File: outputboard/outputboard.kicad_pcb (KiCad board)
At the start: 2 copper layers, 23.5 x 33.9 mm, 12 parts, among them J1 Conn_01x05_Male, J2 AudioJack4, Q1 2N2222A, SW1 SW_SPDT

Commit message: add part description for more complex parts, remove unused cap
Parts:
- D1: value LED_Dual_AAK -> LED_Dual_AAK 2.0/2.2V 20mA
- R4: value 100 -> 120
- R5: value 120 -> 150
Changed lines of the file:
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@@
     (descr "Molex KK-254 Interconnect System, old/engineering part number: AE-6410-05A example for new part number: 22-27-2051, 5 Pins (http://www.molex.com/pdm_docs/sd/022272021_sd.pdf), generated with kicad-footprint-generator")
     (tags "connector Molex KK-254 vertical")
+    (property "Part" "Amtek 2542R-05TW-L")
+    (property "Part (Alt 1)" "JST like JH2.54-5 (Part of X0014J7UB1)")
     (property "Sheetfile" "outputboard.kicad_sch")
     (property "Sheetname" "")
@@
       (effects (font (size 1 1) (thickness 0.15)))
     )
-    (fp_text value "100" (at 0 1.82) (layer "F.Fab")
+    (fp_text value "120" (at 0 1.82) (layer "F.Fab")
       (effects (font (size 1 1) (thickness 0.15)))
     )
@@
   (footprint "outputboard:54-00177" (layer "F.Cu")
     (at 186 105 180)
+    (property "Part" "Tensility 54-00177")
     (property "Sheetfile" "outputboard.kicad_sch")
     (property "Sheetname" "")
@@
   (footprint "outputboard:WS-SLSU" (layer "F.Cu")
     (at 193.5 82.5 -90)
+    (property "Part" "Würth WS-SLSU 450404015514")
     (property "Sheetfile" "outputboard.kicad_sch")
     (property "Sheetname" "")
@@
       (effects (font (size 1 1) (thickness 0.15)))
     )
-    (fp_text value "120" (at 0 1.82) (layer "F.Fab")
+    (fp_text value "150" (at 0 1.82) (layer "F.Fab")
       (effects (font (size 1 1) (thickness 0.15)))
     )
@@
     (descr "SOT-23, Handsoldering")
     (tags "SOT-23")
+    (property "Part" "Nexperia PMBT2222A")
     (property "Sheetfile" "outputboard.kicad_sch")
     (property "Sheetname" "")
@@
     (descr "SOT-23, Handsoldering")
     (tags "SOT-23")
+    (property "Part" "Kingbright KM23ESGW")
     (property "Sheetfile" "outputboard.kicad_sch")
     (property "Sheetname" "")
@@
       (effects (font (size 1 1) (thickness 0.15)) (justify mirror))
     )
-    (fp_text value "LED_Dual_AAK" (at 0 -2.5 90) (layer "B.Fab")
-      (effects (font (size 1 1) (thickness 0.15)) (justify mirror))
-    )
+    (fp_text value "LED_Dual_AAK 2.0/2.2V 20mA" (at 0 -2.5 90) (layer "B.Fab")
+      (effects (font (size 1 1) (thickness 0.15)) (justify mirror))
+    )

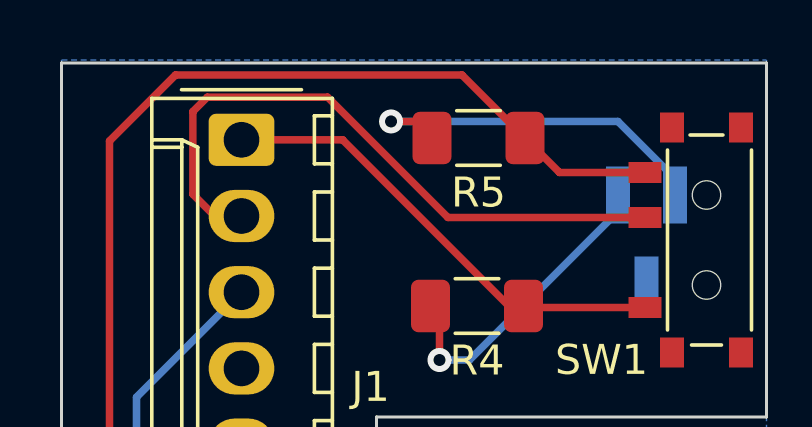
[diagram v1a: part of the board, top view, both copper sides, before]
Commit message: add star to first pin
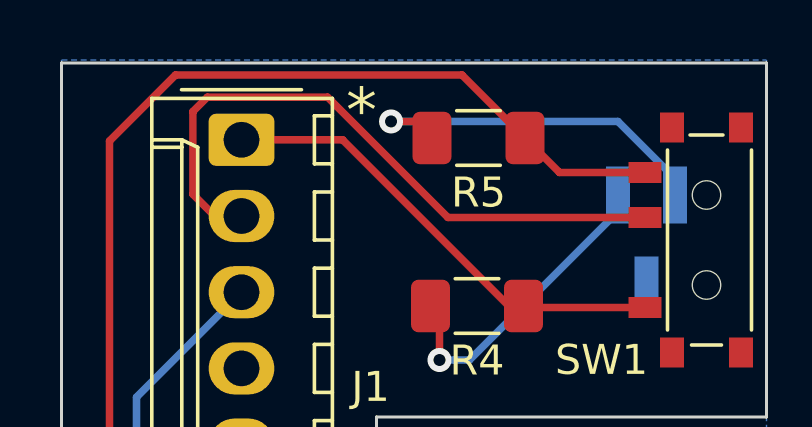
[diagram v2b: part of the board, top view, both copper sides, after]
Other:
- board text added: "*"
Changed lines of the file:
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@@
     (effects (font (size 1 1) (thickness 0.15)))
+  )
+  (gr_text "*" (at 182 78.2) (layer "F.SilkS")
+    (effects (font (size 1.5 1.5) (thickness 0.3)))
   )
   (segment (start 184.6 85) (end 184.3 84.7) (width 0.25) (layer "F.Cu") (net 1))
